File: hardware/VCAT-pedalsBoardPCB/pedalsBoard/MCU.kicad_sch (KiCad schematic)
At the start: 6 parts

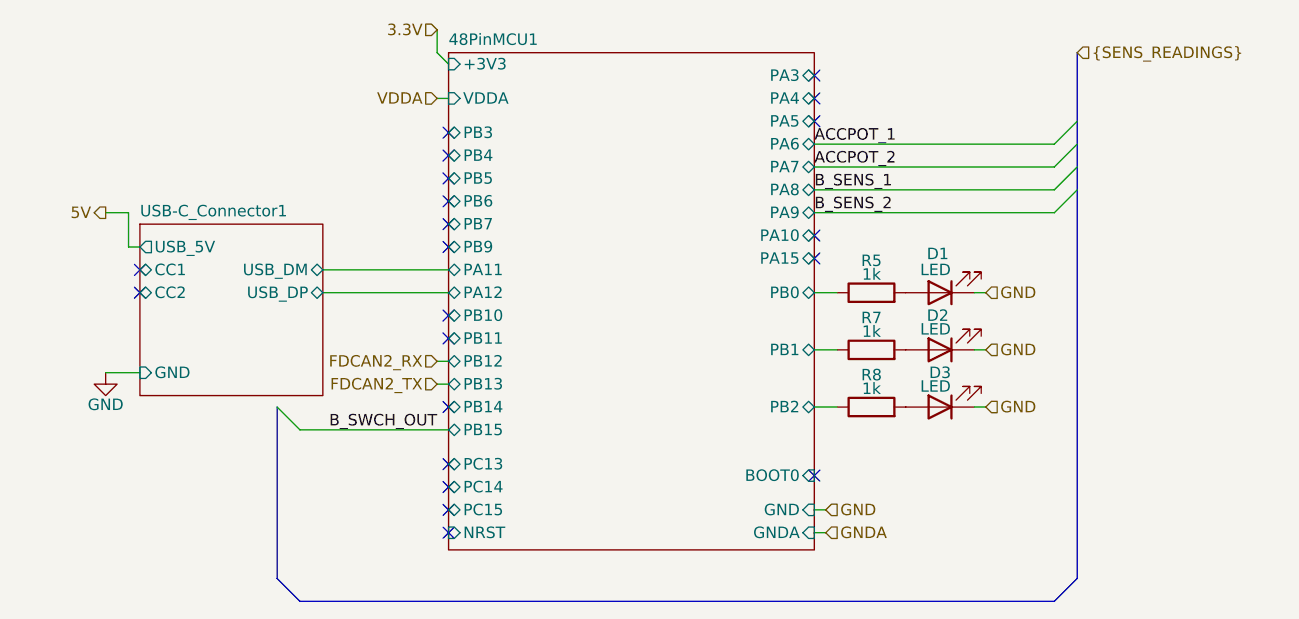
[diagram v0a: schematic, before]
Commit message: addressed review, brake switch on slack
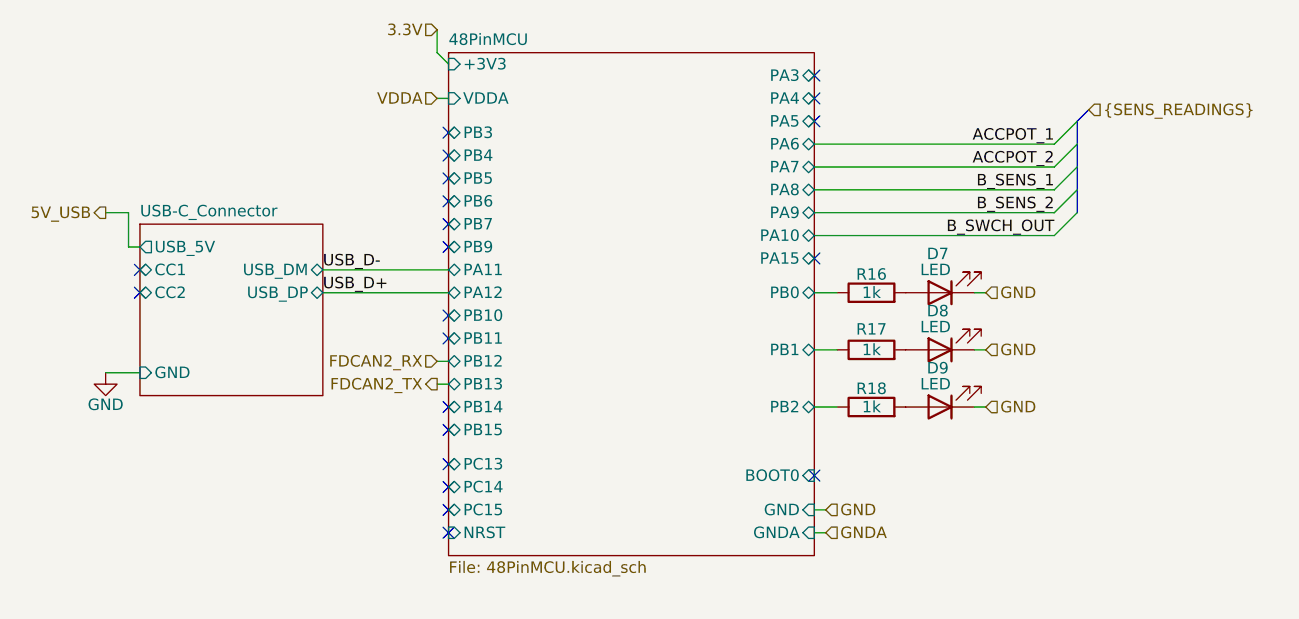
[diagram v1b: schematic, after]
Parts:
- removed D2, D3: LED, symbol Device:LED
- added D8, D9: LED, LHRS_Special:RGB_LED, symbol Device:LED
- D7: renamed from D1; n/p (none) -> LTST-C193KGKT-5A
- renumbered R5 to R16, R7 to R17, R8 to R18
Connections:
- net GND: now also D8.1 (K), D9.1 (K)
- net at R18.2: now also D9.2 (A)
- net at R17.2: now also D8.2 (A)
- net 48PinMCU1/PB0 renamed 48PinMCU/PB0
- net 48PinMCU1/PB1 renamed 48PinMCU/PB1
- net 48PinMCU1/PB2 renamed 48PinMCU/PB2
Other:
- removed sheet 48PinMCU1
- removed sheet USB-C_Connector1
- added sheet 48PinMCU (48PinMCU.kicad_sch)
- added sheet USB-C_Connector (USB-C_Connector.kicad_sch)

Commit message: hopefully final before layout
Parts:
- R16, R17, R18: footprint Resistor_SMD:R_0603_1608Metric -> Resistor_SMD:R_0603_1608Metric_Pad0.98x0.95mm_HandSolder
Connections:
- no-connect marks 21 -> 18
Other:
- sheet USB-C_Connector ports: added USB_D+, USB_D-; removed USB_DM, USB_DP
